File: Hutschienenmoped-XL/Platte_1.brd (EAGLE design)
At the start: 107 x 105.4 mm, 0 parts

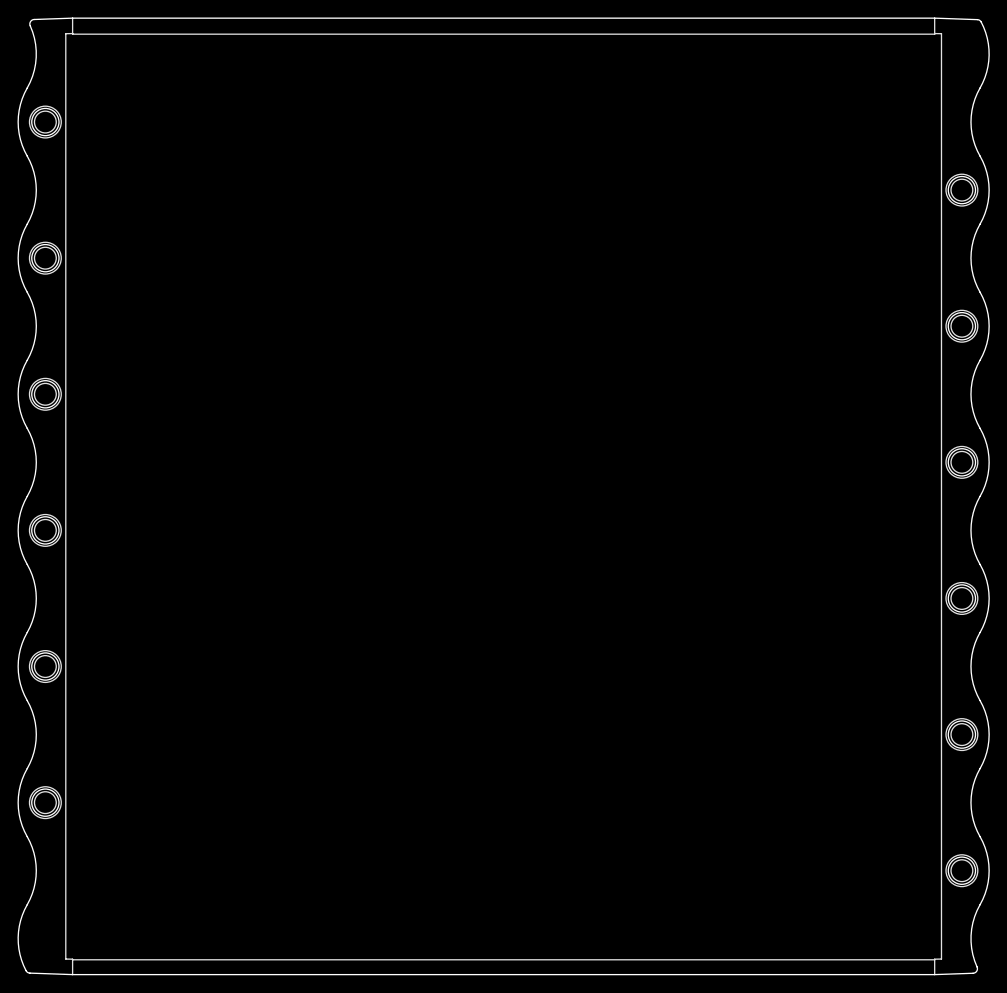
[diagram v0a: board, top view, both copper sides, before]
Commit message: Update grid settings to use millimeters instead of mils, adjust layer visibility, add holes and Fusion synchronization feature compatibility note. Refine circle positions and wire paths in DXF import script.
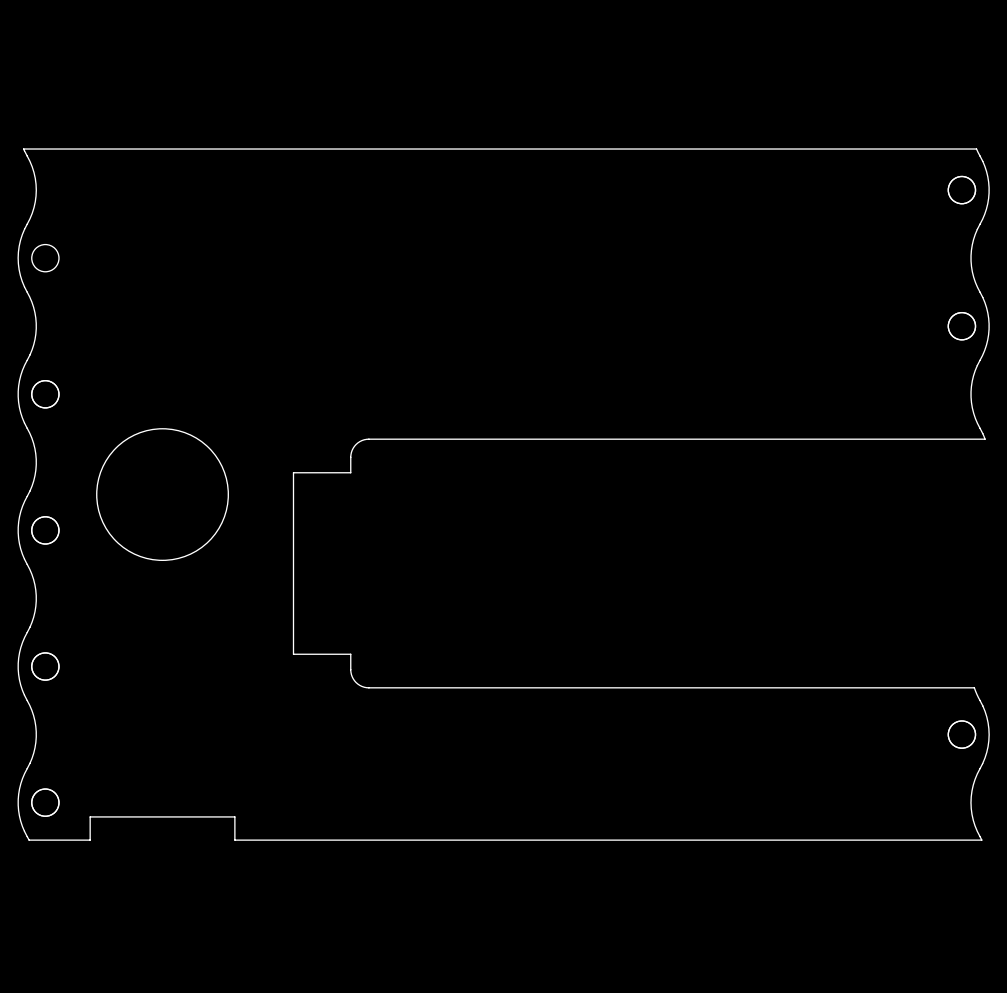
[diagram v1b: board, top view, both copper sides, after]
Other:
- board size 107 x 105.4 mm -> 107 x 76.2 mm
